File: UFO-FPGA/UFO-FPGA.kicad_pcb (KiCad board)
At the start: 6 copper layers, 68.6 x 53.3 mm, 165 parts, among them J1 Power, J2 Digital, J3 Digital/PWM, J4 Digital, J5 USB_B_Micro, Q1 2N7002, SW1 SW_Push_DPDT, SW2 SW_DIP_x01, U1 ICE40HX8K-BG121, U11 TL071, U12 MAX11116AUT+T, U2 FT2232HL, U3 ASDMB-12MHz, U4 MC34063AD, U5 93LC56CT-I/MS, U6 PWR convert, U7 PWR convert, U9 N25Q032A13ESC40F

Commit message: PCB
many pcb changes
-started routing
-added vias
-power planes
-ground planes
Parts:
- removed C14, C25, C26, C27, C28, C33, C34, C35, C36, C5, C6, C63, C68: 100nF, Capacitor_SMD:C_0805_2012Metric_Pad1.18x1.45mm_HandSolder
- removed R37: 12k, Resistor_SMD:R_0805_2012Metric_Pad1.20x1.40mm_HandSolder
- removed R38: 24k, Resistor_SMD:R_0805_2012Metric_Pad1.20x1.40mm_HandSolder
- removed R42: 12k, Resistor_SMD:R_0805_2012Metric
- removed R43: 3k, Resistor_SMD:R_0805_2012Metric
- removed R49: 900, Resistor_SMD:R_0805_2012Metric_Pad1.20x1.40mm_HandSolder
- removed R50: 400, Resistor_SMD:R_0805_2012Metric_Pad1.20x1.40mm_HandSolder
- removed R51: 750R, Resistor_SMD:R_0805_2012Metric
- removed R56: 130R, Resistor_SMD:R_0805_2012Metric_Pad1.20x1.40mm_HandSolder
- C16, C17, C18, R25, TP5, TP6: moved to F.Cu
- C2, C21, C22, C23, C24, C29, C3, C30, C31, C32, C4, C61, C67: value 100nF -> 200nF
- R28: value 510R -> 690R
- R29: value 1R -> 0
- R30, R31, R32: value 1 -> 0
- moved R54 116.2 mm to (64.0, 94.0), turned to 0 degrees
- moved TP6 110.7 mm to (63.5, 110.2), turned to 0 degrees
- moved TP11 109.9 mm to (69.1, 110.2)
- moved C58 108.3 mm to (68.6, 91.2)
- moved C57 106.7 mm to (68.6, 88.2), turned to 0 degrees
- moved U11 104.3 mm to (69.1, 95.0), turned to 0 degrees
- moved TP8 103.8 mm to (63.5, 104.7)
- moved TP10 102.7 mm to (69.1, 101.1), turned to 0 degrees
- moved TP9 100.6 mm to (69.1, 115.8), turned to 0 degrees
- moved TP7 83.3 mm to (63.5, 101.1), turned to 0 degrees
- moved TP5 73.1 mm to (208.9, 120.3), turned to 0 degrees
- moved U4 72.1 mm to (44.3, 109.1)
- moved TP13 68.5 mm to (37.5, 110.4)
- moved R27 68.1 mm to (210.7, 111.3)
- moved D6 67.2 mm to (47.3, 102.5)
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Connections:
- net Net-(RXLED1-A) renamed /USB Programmer/rxled-mid
- net Net-(RXLED1-K) renamed /USB Programmer/rxled out
- net Net-(TXLED1-A) renamed /USB Programmer/txled-mid
- net Net-(TXLED1-K) renamed /USB Programmer/txled out
- net Net-(U2-REF) renamed /USB Programmer/ftd-ref
- net Net-(U2-~{RESET}) renamed /USB Programmer/ftd-reset
- net Net-(U6-EN) renamed /POWER/+1v2en
- net Net-(U6-FB) renamed /POWER/+1v2FB
- net Net-(U6-NR/SS) renamed /POWER/+1v2NR/ss
- net Net-(U7-FB) renamed /POWER/+3V3FB
- net Net-(U7-NR/SS) renamed /POWER/+3v3NR/ss
- C23 pad 1: /BANK 2 IO/VCCIO_2 -> /BANK 3 IO/VCCIO_3
- C24 pad 1: /BANK 2 IO/VCCIO_2 -> /BANK 3 IO/VCCIO_3
- C29 pad 1: / BANK 0 IO/VCCIO_0 -> /BANK 1 IO/VCCIO_1
- C30 pad 1: / BANK 0 IO/VCCIO_0 -> /BANK 1 IO/VCCIO_1
- R28 pad 2: Net-(R28-Pad2) -> ICE_CDONE
- R29 pad 1: +3V3 -> /BANK 1 IO/VCCIO_1
- R29 pad 2: /BANK 2 IO/VCCIO_2 -> +3V3
- R30 pad 1: +3V3 -> /BANK 2 IO/VCCIO_2
- R30 pad 2: /BANK 1 IO/VCCIO_1 -> +3V3
- R31 pad 1: +3V3 -> /BANK 3 IO/VCCIO_3
- R31 pad 2: / BANK 0 IO/VCCIO_0 -> +3V3
- R32 pad 1: +3V3 -> / BANK 0 IO/VCCIO_0
- R32 pad 2: /BANK 3 IO/VCCIO_3 -> +3V3
- U11 pad 1: unconnected-(U11-NULL-Pad1) -> /ADC/Out-tl71
- U11 pad 2: AIN1_O -> -5V
- U11 pad 3: /ADC/In-tl71 -> +5V
- U11 pad 4: -5V -> AIN1_O
- U11 pad 5: unconnected-(U11-NULL-Pad5) -> /ADC/In-tl71
- U6 pad 2: unconnected-(U6-SNS-Pad2) -> +1V2
- U6 pad 9: unconnected-(U6-400mV-Pad9) -> GND
- U7 pad 10: unconnected-(U7-800mV-Pad10) -> GND
- U7 pad 11: unconnected-(U7-1.6V-Pad11) -> GND
- U7 pad 2: unconnected-(U7-SNS-Pad2) -> +3V3
- U7 pad 6: unconnected-(U7-100mV-Pad6) -> GND
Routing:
- net GND: track 0.00 -> 102.2 mm, vias 0 -> 43
- net +3V3: track 0.16 -> 77.8 mm, vias 0 -> 22
- net Vin: track 0.00 -> 41.3 mm, vias 0 -> 1
- net +1V8: track 0.00 -> 34.4 mm, vias 0 -> 4
- net ICE_SS_B: track 0.00 -> 29.1 mm
- net ICE_CDONE: track 0.00 -> 28.4 mm
- net +5V: track 0.00 -> 24.6 mm, vias 0 -> 11
- net ICE_SCK: track 0.00 -> 24.6 mm
- net Flash-MOSI: track 0.00 -> 23.8 mm
- net ICE_CREST: track 0.00 -> 22.8 mm, vias 0 -> 2
- net Flash-MISO: track 0.00 -> 19.6 mm
- net /USB Programmer/FTD-OSCI: track 0.00 -> 19.3 mm
- net /USB Programmer/EE-D: track 0.00 -> 18.0 mm
- net /USB Programmer/EE-DO: track 0.00 -> 16.9 mm
- net DM: track 0.00 -> 16.5 mm, vias 0 -> 2
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- added copper zone on F.Cu, net +1V2
- added copper zone on In3.Cu, net +2V5
- added copper zone on F.Cu, net +3V3
- added copper zone on F.Cu, net +5V
- added copper zone on In3.Cu, net / BANK 0 IO/VCCIO_0
- added copper zone on In3.Cu, net /BANK 1 IO/VCCIO_1
- added copper zone on In3.Cu, net /BANK 2 IO/VCCIO_2
- added copper zone on In3.Cu, net /BANK 3 IO/VCCIO_3
- added copper zone on In3.Cu, net /BANK 4 - SPI Programming/VCCPLL0
- added copper zone on In3.Cu, net /BANK 4 - SPI Programming/VCCPLL1
- added copper zone on F.Cu, net GND

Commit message: pcb update
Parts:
- removed C49: 220pF, Capacitor_SMD:C_0805_2012Metric_Pad1.18x1.45mm_HandSolder
- removed C50, C54: 100uF, Capacitor_SMD:CP_Elec_6.3x7.7
- removed C51: 470uF, Capacitor_SMD:CP_Elec_8x10.5
- removed C52, C53: 100nF, Capacitor_SMD:C_0805_2012Metric_Pad1.18x1.45mm_HandSolder
- removed C57, C58: 100pF, Capacitor_SMD:C_0805_2012Metric_Pad1.18x1.45mm_HandSolder
- removed D5: B140-E3, Diode_SMD:D_SMA
- removed D6: LED, LED_SMD:LED_0805_2012Metric_Pad1.15x1.40mm_HandSolder
- removed L1: 1uH, Inductor_SMD:L_1210_3225Metric_Pad1.42x2.65mm_HandSolder
- removed L2: 180uH, Inductor_SMD:L_1812_4532Metric_Pad1.30x3.40mm_HandSolder
- removed R45: 3, Resistor_SMD:R_0805_2012Metric
- removed R46: 91k, Resistor_SMD:R_0805_2012Metric
- removed R47: 30k, Resistor_SMD:R_0805_2012Metric
- removed R48: 1.6k, Resistor_SMD:R_0805_2012Metric
- removed R52, R53: 510, Resistor_SMD:R_0805_2012Metric
- removed R54: 10, Resistor_SMD:R_0805_2012Metric
- removed TP10, TP11, TP12, TP13, TP6, TP7, TP8, TP9: TestPoint, TestPoint:TestPoint_Pad_1.5x1.5mm
- removed U11: TL071, Package_TO_SOT_SMD:SOT-23-5_HandSoldering
- removed U12: MAX11116AUT+T, Package_TO_SOT_SMD:SOT-23-6_Handsoldering
- removed U4: MC34063AD, Package_SO:SOIC-8_3.9x4.9mm_P1.27mm
- C43, C44, C60, C61, C62, C64, C67, C69, R21, R22, R23, R27: moved to B.Cu
- moved TP5 73.5 mm to (155.9, 69.4)
- moved R27 67.2 mm to (153.8, 75.7)
- moved R22 58.7 mm to (149.2, 74.7), turned to 0 degrees
- moved R21 55.6 mm to (148.5, 81.6)
- moved C69 53.4 mm to (163.6, 68.2), turned to 90 degrees
- moved C43 53.3 mm to (159.6, 68.2), turned to 90 degrees
- moved C60 53.3 mm to (161.6, 68.2), turned to 90 degrees
- moved C67 53.3 mm to (157.6, 68.2), turned to 90 degrees
- moved C62 51.5 mm to (167.7, 68.2), turned to 90 degrees
- moved C44 51.0 mm to (169.8, 68.2), turned to 90 degrees
- moved C64 51.0 mm to (171.9, 68.2), turned to 90 degrees
- moved C61 45.6 mm to (165.7, 68.2), turned to 90 degrees
- moved TP4 42.8 mm to (131.8, 85.5), turned to 90 degrees
- moved R23 32.4 mm to (158.4, 85.3)
- moved R24 9.78 mm to (149.6, 88.4)
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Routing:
- net GND: track 102.2 -> 154.1 mm, vias 43 -> 53
- net +3V3: track 77.8 -> 114.1 mm, vias 22 -> 24
- net +1V2: track 2.98 -> 36.3 mm, vias 7 -> 12
- net /BANK 4 - SPI Programming/ICE_MISO: track 0.00 -> 24.7 mm, vias 0 -> 1
- net /BANK 4 - SPI Programming/ICE_MOSI: track 0.00 -> 24.4 mm, vias 0 -> 1
- net ICE_SS_B: track 29.1 -> 46.9 mm, vias 0 -> 2
- net ICE_SCK: track 24.6 -> 40.0 mm, vias 0 -> 4
- net Flash-MOSI: track 23.8 -> 39.1 mm, vias 0 -> 2
- net /BANK 4 - SPI Programming/N25-CS: track 0.00 -> 12.8 mm
- net Flash-MISO: track 19.6 -> 27.0 mm
- net ICE_CREST: track 22.8 -> 30.1 mm
- net /BANK 4 - SPI Programming/N25-WP: track 0.00 -> 5.67 mm, vias 0 -> 1
- net /BANK 4 - SPI Programming/N25-HOLD: track 0.00 -> 4.26 mm, vias 0 -> 1
- net /BANK 4 - SPI Programming/VCCPLL0: track 5.84 -> 8.28 mm
- net DCDn: track 8.42 -> 10.3 mm
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
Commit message: DRC run
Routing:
- net +3V3: track 114.1 -> 122.2 mm
- net Vin: track 41.3 -> 43.3 mm
- net GND: track 154.1 -> 155.7 mm, vias 53 -> 54

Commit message: pcb prog redesign
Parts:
- removed SW1: SW_Push_DPDT, Button_Switch_THT:SW_CuK_JS202011CQN_DPDT_Straight
- removed SW2: SW_DIP_x01, Button_Switch_SMD:SW_DIP_SPSTx01_Slide_9.78x4.72mm_W8.61mm_P2.54mm
- added J6: Conn_02x02_Counter_Clockwise, Connector_PinHeader_2.54mm:PinHeader_2x02_P2.54mm_Vertical, F.Cu at (152.2, 83.8)
- added JP1: Jumper_2_Open, Connector_PinHeader_2.54mm:PinHeader_1x02_P2.54mm_Vertical, F.Cu at (152.3, 80.1)
- C16, C17, C18, C21, C22, C29, C30, C31, C32, R10, R11, R12, R13, R25, R29, R32, R8, R9, TP5: moved to B.Cu
- D1, R22: moved to F.Cu
- J5: footprint Connector_USB:USB_Micro-AB_Molex_47590-0001 -> Connector_USB:USB_Micro-B_GCT_USB3076-30-A
- moved R22 18.7 mm to (148.6, 93.5), turned to 90 degrees
- moved R8 18.2 mm to (146.2, 87.5), turned to 180 degrees
- moved R9 15.2 mm to (146.3, 84.2), turned to 180 degrees
- moved R10 12.5 mm to (146.2, 81.5), turned to 180 degrees
- moved R24 11.4 mm to (152.3, 77.3), turned to 0 degrees
- moved U9 11.4 mm to (154.0, 92.2), turned to 180 degrees
- moved R21 10.9 mm to (159.4, 80.6), turned to 90 degrees
- moved R11 10.4 mm to (146.2, 79.0), turned to 180 degrees
- moved R13 9.30 mm to (146.3, 73.0), turned to 180 degrees
- moved R12 8.90 mm to (146.2, 76.8), turned to 180 degrees
- moved FB1 8.70 mm to (119.5, 71.1)
- moved C39 7.75 mm to (125.0, 73.0), turned to -90 degrees
- moved R16 5.61 mm to (150.2, 63.4)
- moved R17 5.61 mm to (150.2, 61.4)
- moved R18 5.61 mm to (150.2, 59.4)
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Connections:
- net DM renamed D-
- net DP renamed D+
- J1 pad 1: Vin -> PIN-22
- J1 pad 2: PIN-22 -> PIN-23
- J1 pad 3: PIN-23 -> PIN-24
- U1 pad K6: unconnected-(U1C-IOB_82_GBIN4-PadK6) -> ICE_CLK
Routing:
- net Vin: track 43.3 -> 4.12 mm, vias 1 -> 0
- net ICE_SS_B: track 46.9 -> 16.6 mm, vias 2 -> 1
- net Flash-MOSI: track 39.1 -> 10.2 mm, vias 2 -> 0
- net /USB Programmer/ICE-CDONE: track 4.64 -> 25.9 mm, vias 0 -> 1
- net /USB Programmer/FLASH_MISO: track 3.55 -> 22.9 mm, vias 0 -> 1
- net /USB Programmer/ICE-SS-B: track 3.75 -> 22.9 mm, vias 0 -> 1
- net /USB Programmer/FLASH_MOSI: track 4.11 -> 22.9 mm, vias 0 -> 1
- net /USB Programmer/ICE-CREST: track 5.99 -> 23.2 mm, vias 0 -> 1
- net /USB Programmer/ICE-SCK: track 5.75 -> 22.9 mm, vias 0 -> 1
- net ICE_SCK: track 40.0 -> 25.2 mm, vias 4 -> 2
- net ICE_CLK: track 0.00 -> 14.2 mm
- net /BANK 4 - SPI Programming/ICE_MOSI: track 24.4 -> 12.0 mm
- net ICE_CREST: track 30.1 -> 17.9 mm, vias 2 -> 1
- net GND: track 155.7 -> 167.5 mm, vias 54 -> 61
- net /BANK 4 - SPI Programming/ICE_MISO: track 24.7 -> 13.0 mm
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- added copper zone on In2.Cu, net +1V2
- added copper zone on In2.Cu, net +2V5
- added copper zone on In2.Cu, net +3V3
- added copper zone on In2.Cu, net +5V
- added copper zone on In2.Cu, net / BANK 0 IO/VCCIO_0
- added copper zone on In2.Cu, net /BANK 1 IO/VCCIO_1
- added copper zone on In2.Cu, net /BANK 2 IO/VCCIO_2
- added copper zone on In2.Cu, net /BANK 3 IO/VCCIO_3
- added copper zone on In2.Cu, net /BANK 4 - SPI Programming/VCCPLL0
- added copper zone on In2.Cu, net /BANK 4 - SPI Programming/VCCPLL1
- added copper zone on B.Cu, net GND
- removed copper zone on In3.Cu, net +1V2
- removed copper zone on In3.Cu, net +2V5
- removed copper zone on In3.Cu, net +3V3
- removed copper zone on In3.Cu, net +5V
- removed copper zone on In3.Cu, net / BANK 0 IO/VCCIO_0
- removed copper zone on In3.Cu, net /BANK 1 IO/VCCIO_1
- removed copper zone on In3.Cu, net /BANK 2 IO/VCCIO_2
- removed copper zone on In3.Cu, net /BANK 3 IO/VCCIO_3
- removed copper zone on In3.Cu, net /BANK 4 - SPI Programming/VCCPLL0
- removed copper zone on In3.Cu, net /BANK 4 - SPI Programming/VCCPLL1
- removed copper zone on In4.Cu, net GND
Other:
- outline, holes or cut-outs redrawn
- copper layers 6 -> 4

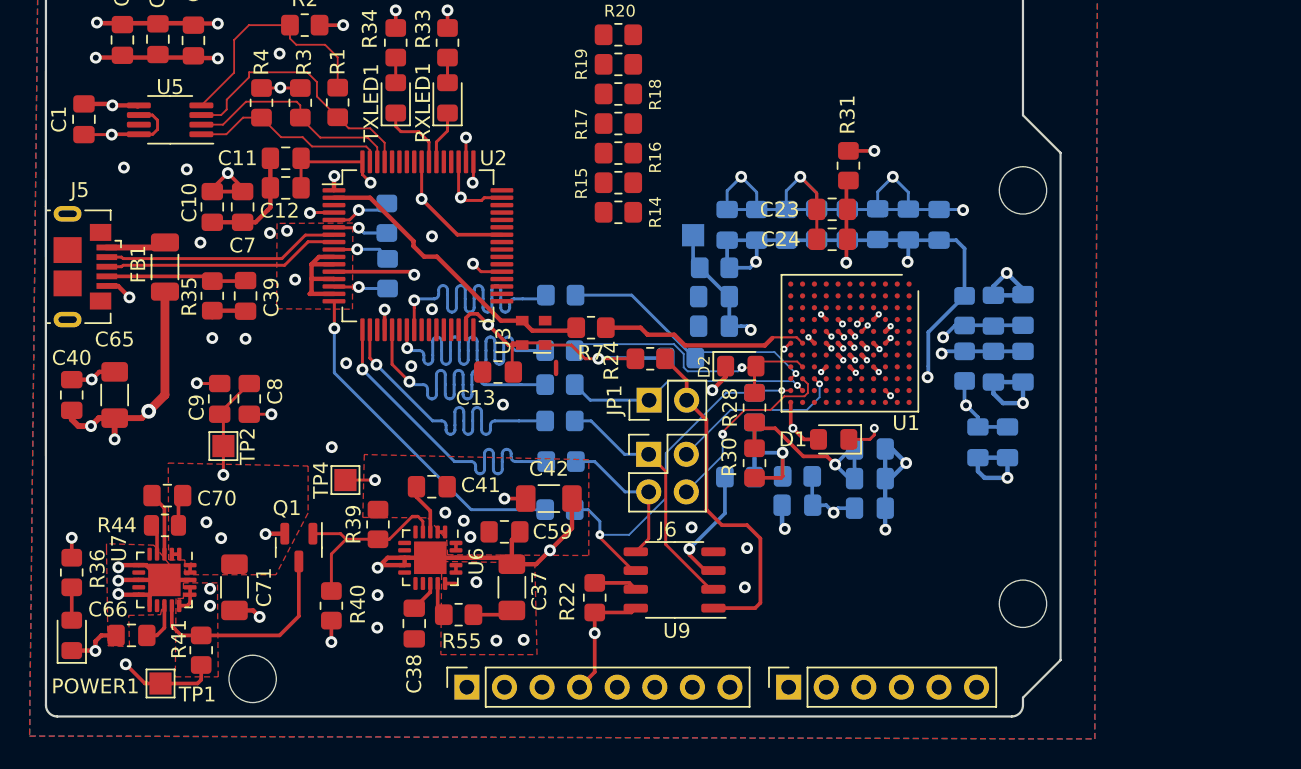
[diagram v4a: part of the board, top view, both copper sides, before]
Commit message: pcb placement
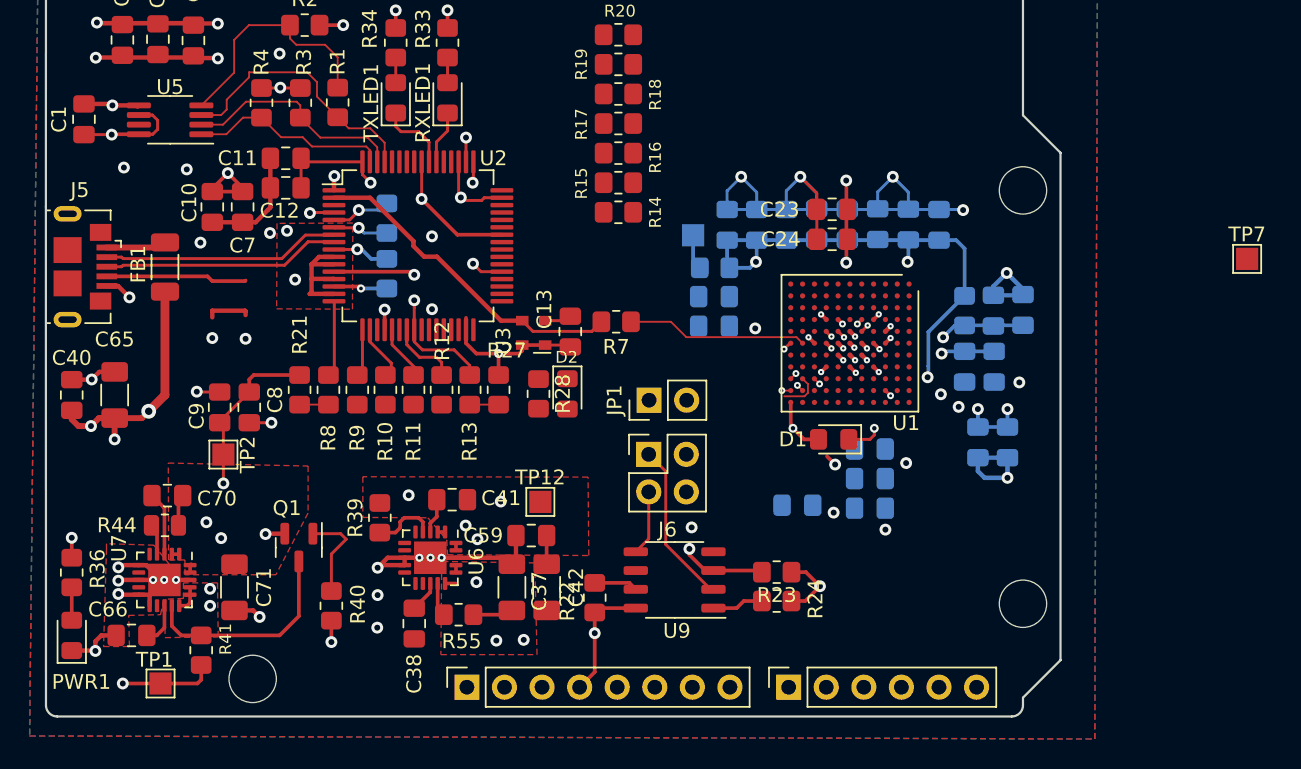
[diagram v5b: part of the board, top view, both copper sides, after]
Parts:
- removed C39: 100nF, Capacitor_SMD:C_0805_2012Metric_Pad1.18x1.45mm_HandSolder
- removed R29, R30, R31, R32, R35: 0, Resistor_SMD:R_0805_2012Metric_Pad1.20x1.40mm_HandSolder
- removed TP4: TestPoint, TestPoint:TestPoint_Pad_1.5x1.5mm
- added TP12: TestPoint, TestPoint:TestPoint_Pad_1.5x1.5mm, F.Cu at (144.9, 87.0)
- added TP7: TestPoint, TestPoint:TestPoint_Pad_1.5x1.5mm, F.Cu at (192.7, 70.5)
- R10, R11, R12, R13, R21, R23, R27, R8, R9: moved to F.Cu
- moved R21 30.8 mm to (128.7, 79.4), turned to -90 degrees
- moved R24 18.5 mm to (160.9, 93.7), turned to 180 degrees
- moved R8 17.6 mm to (130.6, 79.4), turned to 90 degrees
- moved R28 14.6 mm to (144.8, 79.7), turned to -90 degrees
- moved R9 14.6 mm to (132.6, 79.4), turned to 90 degrees
- moved R27 12.5 mm to (142.1, 79.4), turned to -90 degrees
- moved R10 12.0 mm to (134.4, 79.4), turned to 90 degrees
- moved D2 11.9 mm to (146.8, 79.7), turned to -90 degrees
- moved R11 9.91 mm to (136.3, 79.4), turned to 90 degrees
- moved R13 8.88 mm to (140.2, 79.4), turned to 90 degrees
- moved R12 8.43 mm to (138.2, 79.4), turned to 90 degrees
- moved R23 6.89 mm to (160.9, 91.7)
- moved C42 6.00 mm to (145.3, 92.8), turned to -90 degrees
- moved C13 5.60 mm to (146.9, 75.5), turned to 90 degrees
- moved C31 1.95 mm to (173.6, 77.8)
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- renumbered POWER1 to PWR1
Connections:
- C21 pad 1: /BANK 2 IO/VCCIO_2 -> +3V3
- C22 pad 1: /BANK 2 IO/VCCIO_2 -> +3V3
- C23 pad 1: /BANK 3 IO/VCCIO_3 -> +3V3
- C24 pad 1: /BANK 3 IO/VCCIO_3 -> +3V3
- C29 pad 1: /BANK 1 IO/VCCIO_1 -> +3V3
- C30 pad 1: /BANK 1 IO/VCCIO_1 -> +3V3
- C31 pad 1: / BANK 0 IO/VCCIO_0 -> +3V3
- C32 pad 1: / BANK 0 IO/VCCIO_0 -> +3V3
- J5 pad 4: Net-(J5-ID) -> unconnected-(J5-ID-Pad4)
- R28 pad 1: /BANK 2 IO/VCCIO_2 -> +3V3
- U1 pad D6: / BANK 0 IO/VCCIO_0 -> +3V3
- U1 pad E4: /BANK 3 IO/VCCIO_3 -> +3V3
- U1 pad F8: /BANK 1 IO/VCCIO_1 -> +3V3
- U1 pad G4: /BANK 3 IO/VCCIO_3 -> +3V3
- U1 pad H6: /BANK 2 IO/VCCIO_2 -> +3V3
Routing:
- net GND: track 167.5 -> 142.0 mm, vias 61 -> 60
- net ICE_SCK: track 25.2 -> 2.74 mm, vias 2 -> 1
- net /USB Programmer/ICE-CDONE: track 25.9 -> 4.73 mm, vias 1 -> 0
- net /USB Programmer/FLASH_MOSI: track 22.9 -> 2.88 mm, vias 1 -> 0
- net /BANK 4 - SPI Programming/N25-CS: track 23.5 -> 3.47 mm
- net /USB Programmer/FLASH_MISO: track 22.9 -> 3.46 mm, vias 1 -> 0
- net /USB Programmer/ICE-SS-B: track 22.9 -> 3.63 mm, vias 1 -> 0
- net ICE_CDONE: track 18.9 -> 0.00 mm, vias 1 -> 0
- net /USB Programmer/ICE-SCK: track 22.9 -> 4.80 mm, vias 1 -> 0
- net ICE_SS_B: track 16.6 -> 0.49 mm
- net ICE_CREST: track 17.9 -> 2.44 mm
- net /USB Programmer/ICE-CREST: track 23.2 -> 7.86 mm
- net /BANK 2 IO/VCCIO_2: track 14.2 -> 0.00 mm, vias 2 -> 0
- net /BANK 4 - SPI Programming/ICE_MOSI: track 12.0 -> 0.49 mm
- net /BANK 4 - SPI Programming/ICE_MISO: track 13.0 -> 2.80 mm, vias 1 -> 0
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- removed copper zone on In2.Cu, net / BANK 0 IO/VCCIO_0
- removed copper zone on In2.Cu, net /BANK 1 IO/VCCIO_1
- removed copper zone on In2.Cu, net /BANK 2 IO/VCCIO_2
- removed copper zone on In2.Cu, net /BANK 3 IO/VCCIO_3
